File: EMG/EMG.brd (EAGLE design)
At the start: 70 x 39 mm, 57 parts, among them IC1 TL074CD, IC2 TL074CD, IC3 TL074CD, J1 SJ-3523-SMT-TR, J3 640455-5

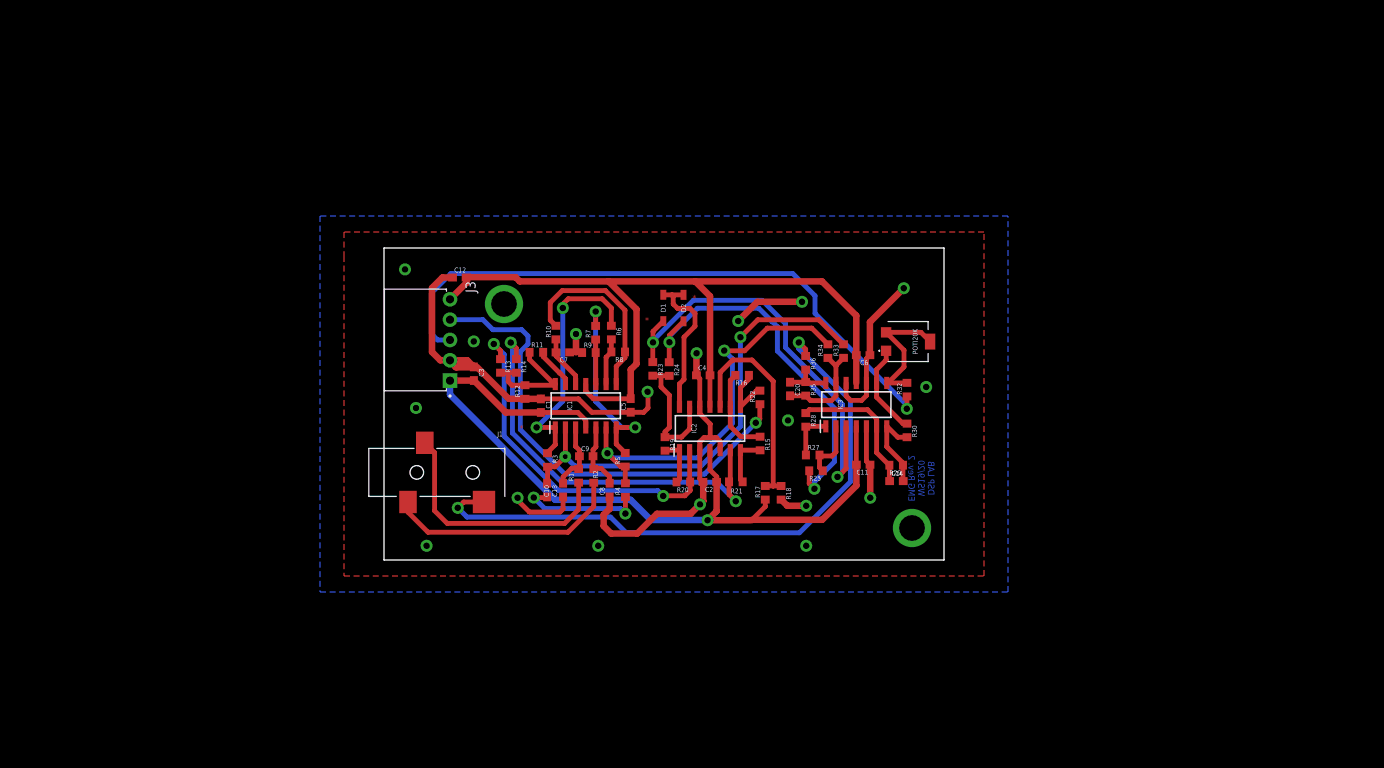
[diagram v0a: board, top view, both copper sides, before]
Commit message: Added pictures for EMG and Mainboard for final report
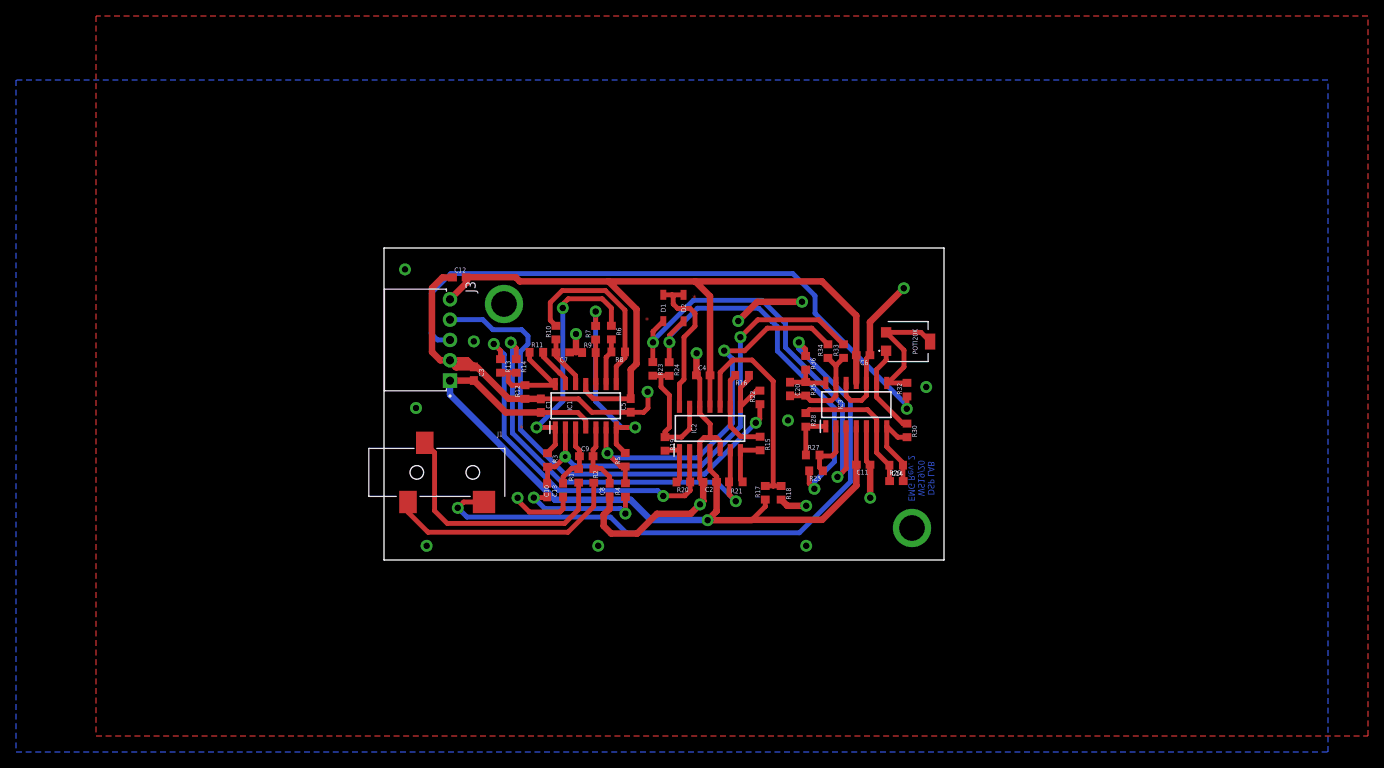
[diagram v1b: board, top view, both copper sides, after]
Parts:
- R13, R14, R20, R21: value ZERO -> 10k
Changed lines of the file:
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@@
 <?xml version="1.0" encoding="utf-8"?>
 <!DOCTYPE eagle SYSTEM "eagle.dtd">
-<eagle version="9.5.2">
+<eagle version="9.6.2">
 <drawing>
 <settings>
@@
 <grid distance="1" unitdist="mm" unit="mm" style="lines" multiple="1" display="yes" altdistance="0.025" altunitdist="mm" altunit="mm"/>
 <layers>
-<layer number="1" name="Top" color="4" fill="1" visible="yes" active="yes"/>
+<layer number="1" name="Top" color="4" fill="1" visible="no" active="yes"/>
 <layer number="2" name="Route2" color="16" fill="1" visible="no" active="no"/>
 <layer number="3" name="Route3" color="17" fill="1" visible="no" active="no"/>
@@
 <layer number="19" name="Unrouted" color="6" fill="1" visible="yes" active="yes"/>
 <layer number="20" name="Dimension" color="14" fill="1" visible="yes" active="yes"/>
-<layer number="21" name="tPlace" color="7" fill="1" visible="yes" active="yes"/>
+<layer number="21" name="tPlace" color="7" fill="1" visible="no" active="yes"/>
 <layer number="22" name="bPlace" color="7" fill="1" visible="yes" active="yes"/>
-<layer number="23" name="tOrigins" color="15" fill="1" visible="yes" active="yes"/>
+<layer number="23" name="tOrigins" color="15" fill="1" visible="no" active="yes"/>
 <layer number="24" name="bOrigins" color="15" fill="1" visible="yes" active="yes"/>
-<layer number="25" name="tNames" color="7" fill="1" visible="yes" active="yes"/>
+<layer number="25" name="tNames" color="7" fill="1" visible="no" active="yes"/>
 <layer number="26" name="bNames" color="7" fill="1" visible="yes" active="yes"/>
-<layer number="27" name="tValues" color="7" fill="1" visible="yes" active="yes"/>
+<layer number="27" name="tValues" color="7" fill="1" visible="no" active="yes"/>
 <layer number="28" name="bValues" color="7" fill="1" visible="yes" active="yes"/>
-<layer number="29" name="tStop" color="7" fill="3" visible="yes" active="yes"/>
+<layer number="29" name="tStop" color="7" fill="3" visible="no" active="yes"/>
 <layer number="30" name="bStop" color="7" fill="6" visible="yes" active="yes"/>
-<layer number="31" name="tCream" color="7" fill="4" visible="yes" active="yes"/>
+<layer number="31" name="tCream" color="7" fill="4" visible="no" active="yes"/>
 <layer number="32" name="bCream" color="7" fill="5" visible="yes" active="yes"/>
-<layer number="33" name="tFinish" color="6" fill="3" visible="yes" active="yes"/>
+<layer number="33" name="tFinish" color="6" fill="3" visible="no" active="yes"/>
 <layer number="34" name="bFinish" color="6" fill="6" visible="yes" active="yes"/>
-<layer number="35" name="tGlue" color="7" fill="4" visible="yes" active="yes"/>
+<layer number="35" name="tGlue" color="7" fill="4" visible="no" active="yes"/>
 <layer number="36" name="bGlue" color="7" fill="5" visible="yes" active="yes"/>
-<layer number="37" name="tTest" color="7" fill="1" visible="yes" active="yes"/>
+<layer number="37" name="tTest" color="7" fill="1" visible="no" active="yes"/>
 <layer number="38" name="bTest" color="7" fill="1" visible="yes" active="yes"/>
-<layer number="39" name="tKeepout" color="4" fill="11" visible="yes" active="yes"/>
+<layer number="39" name="tKeepout" color="4" fill="11" visible="no" active="yes"/>
 <layer number="40" name="bKeepout" color="1" fill="11" visible="yes" active="yes"/>
-<layer number="41" name="tRestrict" color="4" fill="10" visible="yes" active="yes"/>
+<layer number="41" name="tRestrict" color="4" fill="10" visible="no" active="yes"/>
 <layer number="42" name="bRestrict" color="1" fill="10" visible="yes" active="yes"/>
-<layer number="43" name="vRestrict" color="2" fill="10" visible="yes" active="yes"/>
+<layer number="43" name="vRestrict" color="2" fill="10" visible="no" active="yes"/>
 <layer number="44" name="Drills" color="7" fill="1" visible="yes" active="yes"/>
 <layer number="45" name="Holes" color="7" fill="1" visible="yes" active="yes"/>
-<layer number="46" name="Milling" color="3" fill="1" visible="yes" active="yes"/>
-<layer number="47" name="Measures" color="7" fill="1" visible="yes" active="yes"/>
-<layer number="48" name="Document" color="7" fill="1" visible="yes" active="yes"/>
-<layer number="49" name="Reference" color="7" fill="1" visible="yes" active="yes"/>
-<layer number="51" name="tDocu" color="7" fill="1" visible="yes" active="yes"/>
+<layer number="46" name="Milling" color="3" fill="1" visible="no" active="yes"/>
+<layer number="47" name="Measures" color="7" fill="1" visible="no" active="yes"/>
+<layer number="48" name="Document" color="7" fill="1" visible="no" active="yes"/>
+<layer number="49" name="Reference" color="7" fill="1" visible="no" active="yes"/>
+<layer number="51" name="tDocu" color="7" fill="1" visible="no" active="yes"/>
 <layer number="52" name="bDocu" color="7" fill="1" visible="yes" active="yes"/>
 <layer number="88" name="SimResults" color="9" fill="1" visible="no" active="no"/>
@@
 </layers>
 <board>
-<fusionsync huburn="a.cGVyc29uYWw6dWUyYjYwNWI1" projecturn="a.cGVyc29uYWw6dWUyYjYwNWI1IzIwMTcwNjI4ODIwMDY4MjY" f3durn="urn:adsk.wipprod:dm.lineage:ZbhE2_fPTCeosJ1NQofmUQ" pcbguid="7141c638-896e-4bdd-87cb-a4c95d91adb6" lastpulledtime="" lastsyncedchangeguid="8f1454f7-6113-cbcb-b36a-77c0ec95b333"/>
+<fusionsync huburn="a.cGVyc29uYWw6dWUyYjYwNWI1" projecturn="a.cGVyc29uYWw6dWUyYjYwNWI1IzIwMTcwNjI4ODIwMDY4MjY" f3durn="urn:adsk.wipprod:dm.lineage:ZbhE2_fPTCeosJ1NQofmUQ" pcbguid="7141c638-896e-4bdd-87cb-a4c95d91adb6" lastpulledtime="" lastsyncedchangeguid="8f1454f7-6113-cbcb-b36a-77c0ec95b333" latestrevisionid="" lastsyncedrevisionid="" lastboardhashguid="" lastpushedtime="" linktopcb3d="false"/>
 <plain>
 <wire x1="-40" y1="-25" x2="30" y2="-25" width="0" layer="20"/>
@@
 <attribute name="VALUE" x="-23.11" y="-3.71" size="0.6096" layer="27" rot="R180"/>
 </element>
-<element name="R13" library="rcl" library_urn="urn:adsk.eagle:library:334" package="R0603" package3d_urn="urn:adsk.eagle:package:23555/3" value="ZERO" x="-25.44" y="-0.74" smashed="yes" rot="R270">
+<element name="R13" library="rcl" library_urn="urn:adsk.eagle:library:334" package="R0603" package3d_urn="urn:adsk.eagle:package:23555/3" value="10k" x="-25.44" y="-0.74" smashed="yes" rot="R270">
 <attribute name="NAME" x="-24.805" y="-0.105" size="0.6096" layer="25" rot="R270"/>
 <attribute name="POPULARITY" value="70" x="-25.44" y="-0.74" size="1.778" layer="27" rot="R270" display="off"/>
@@
 <attribute name="VALUE" x="-27.345" y="-0.105" size="0.6096" layer="27" rot="R270"/>
 </element>
-<element name="R14" library="rcl" library_urn="urn:adsk.eagle:library:334" package="R0603" package3d_urn="urn:adsk.eagle:package:23555/3" value="ZERO" x="-23.465" y="-0.74" smashed="yes" rot="R270">
+<element name="R14" library="rcl" library_urn="urn:adsk.eagle:library:334" package="R0603" package3d_urn="urn:adsk.eagle:package:23555/3" value="10k" x="-23.465" y="-0.74" smashed="yes" rot="R270">
 <attribute name="NAME" x="-22.83" y="-0.105" size="0.6096" layer="25" rot="R270"/>
 <attribute name="POPULARITY" value="70" x="-23.465" y="-0.74" size="1.778" layer="27" rot="R270" display="off"/>
@@
 <attribute name="VALUE" x="-15.685" y="-13.85" size="0.6096" layer="27" rot="R270"/>
 </element>
-<element name="R20" library="rcl" library_urn="urn:adsk.eagle:library:334" package="R0603" package3d_urn="urn:adsk.eagle:package:23555/3" value="ZERO" x="-2.58" y="-15.245" smashed="yes">
+<element name="R20" library="rcl" library_urn="urn:adsk.eagle:library:334" package="R0603" package3d_urn="urn:adsk.eagle:package:23555/3" value="10k" x="-2.58" y="-15.245" smashed="yes">
 <attribute name="NAME" x="-3.39" y="-16.535" size="0.6096" layer="25"/>
 <attribute name="POPULARITY" value="70" x="-2.58" y="-15.245" size="1.778" layer="27" display="off"/>
@@
 <attribute name="VALUE" x="-3.665" y="-17.2" size="0.6096" layer="27"/>
 </element>
-<element name="R21" library="rcl" library_urn="urn:adsk.eagle:library:334" package="R0603" package3d_urn="urn:adsk.eagle:package:23555/3" value="ZERO" x="3.98" y="-15.23" smashed="yes" rot="R180">
+<element name="R21" library="rcl" library_urn="urn:adsk.eagle:library:334" package="R0603" package3d_urn="urn:adsk.eagle:package:23555/3" value="10k" x="3.98" y="-15.23" smashed="yes" rot="R180">
 <attribute name="NAME" x="4.815" y="-16.065" size="0.6096" layer="25" rot="R180"/>
 <attribute name="POPULARITY" value="70" x="3.98" y="-15.23" size="1.778" layer="27" rot="R180" display="off"/>
@@
 <wire x1="-20.395" y1="-4.855" x2="-20.39" y2="-4.86" width="0.8128" layer="1"/>
 <polygon width="0.8128" layer="1" isolate="0.8128">
-<vertex x="-45" y="13"/>
-<vertex x="-45" y="-27"/>
-<vertex x="35" y="-27"/>
-<vertex x="35" y="16"/>
-<vertex x="-45" y="16"/>
+<vertex x="-76" y="43"/>
+<vertex x="-76" y="-47"/>
+<vertex x="83" y="-47"/>
+<vertex x="83" y="43"/>
 </polygon>
 <polygon width="0.8128" layer="16" isolate="0.8128">
-<vertex x="-48" y="18"/>
-<vertex x="-48" y="-29"/>
-<vertex x="38" y="-29"/>
-<vertex x="38" y="18"/>
+<vertex x="-86" y="35"/>
+<vertex x="-86" y="-49"/>
+<vertex x="78" y="-49"/>
+<vertex x="78" y="35"/>
 </polygon>
 <via x="-7.05" y="-3.975" extent="1-16" drill="0.8" diameter="1.5"/>
